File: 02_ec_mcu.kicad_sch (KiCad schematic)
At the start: 48 parts, among them J16 Case power/reset button harne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, J4 TC2030 Cortex SWD: VTref/SWDI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, SW1 Reset, SW4 BOOT0 (DFU), U4 STM32F407VGTx, U44 TCA9539PWR resettable source 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, U46 SN74LVC1G08DBVR EC-reset-qual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, U5 TPS54202DDC, Y1 J32SMX-K-F-G-I-8M0 8MHz CL8pF, Y2 X1A000141000612 32.768kHz CL6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

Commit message: Independent-verifier sweep: fix 12 stale contracts + 4 real board bugs
The full independent verification suite (not just the schematic gate)
caught real issues before routing:

Contracts/verifiers fixed (9 stale expectations that would have masked
regressions):
- U44 pin 9: SOURCE_MGR_SPARE2 -> SLS_S3 (contracts + closure)
- U61 pins 1/3/7: GND/NC -> EC_DFU_SEL / DFU DP/DM (DFU rework)
- C832 + U772 pins 1/2/4: SYS_3V3 -> PCIE_3V3_IN (endpoint buck)
- J2300: full 60-pin -> verified 30-pin FH12 map (contracts + pin review)
- J9 RTC header block -> D1824/C783 diode-OR block
- U63/R203 obsolete expectations (refs reused for the DFU parts)

Real board bugs found and fixed:
- J11 right-edge USB-C misplaced 6 mm inside the edge (shell pad would
  never align with the chassis cutout); moved to mirror J12 at x 353.48
- R207 fan PWM series resistor stranded at the right edge (shorted
  J11's shell); relocated under the NVMe card (height-legal), clear of
  the charger/mux clusters
- C35 placed inside the Ethernet notch void (would be routed off);
  moved to x 348
- BOM: 11 new parts missing Manufacturer/MPN stamps -> catalog entries
  added; BOM gate now PASS (0 gaps)

Release gate now: DRC all allowlisted (courtyards 165, silk 8+1),
schematic parity 0, pin review 2575 PASS / 0 FAIL, closure 1605/0,
calcs 123/0, off-board anchors 0. Remaining FAILs are expected:
stackup PENDING_NEXTPCB (awaiting fab reply) and 499 unrouted.
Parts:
- R212: MPN (none) -> RC0603FR-071KL; Manufacturer (none) -> Yageo
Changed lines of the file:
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@@
   (property "Footprint" "Resistor_SMD:R_0603_1608Metric" (at 20.32 229.87 0) (effects (font (size 1.27 1.27)) (hide yes)))
   (property "Datasheet" "" (at 20.32 229.87 0) (effects (font (size 1.27 1.27)) (hide yes)))
+  (property "Manufacturer" "Yageo" (at 20.32 229.87 0) (effects (font (size 1.27 1.27)) (hide yes)))
+  (property "MPN" "RC0603FR-071KL" (at 20.32 229.87 0) (effects (font (size 1.27 1.27)) (hide yes)))
   (pin "1")
   (pin "2")

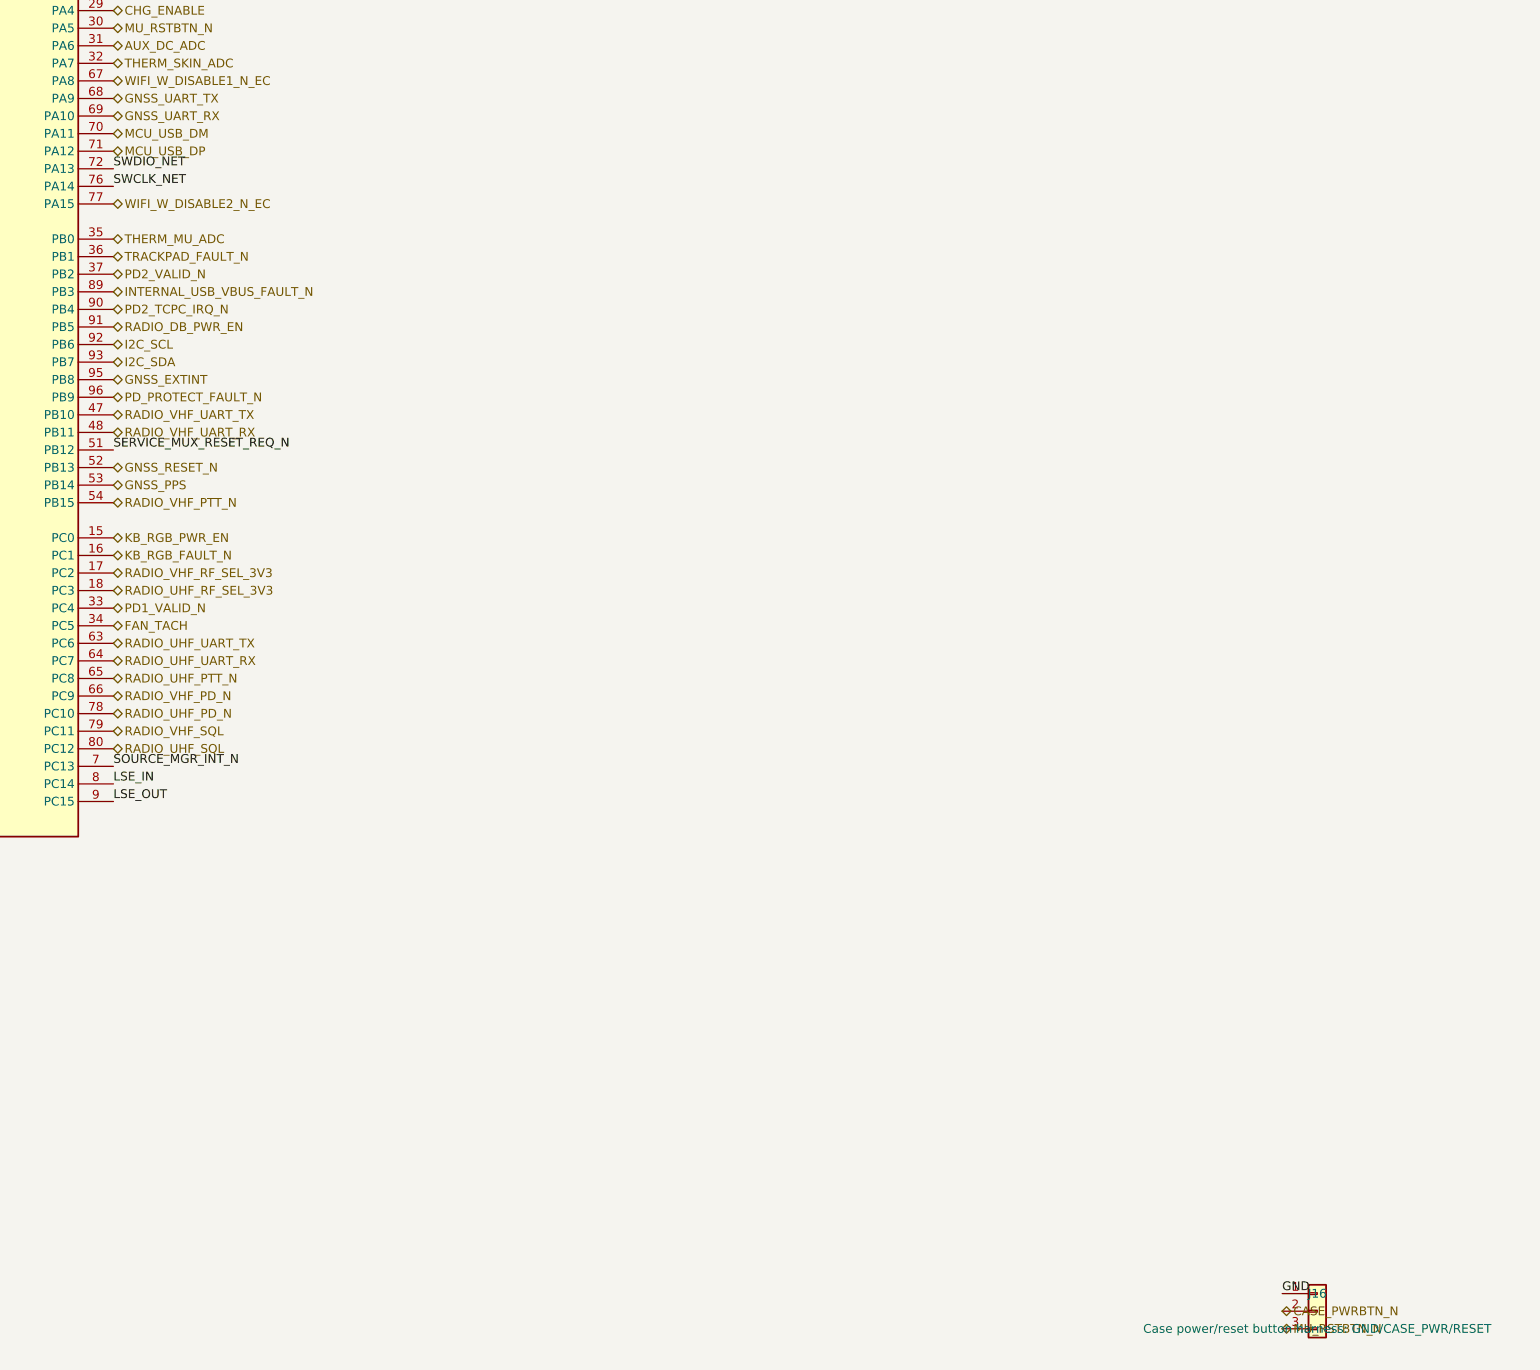
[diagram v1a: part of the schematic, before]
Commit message: get the main boards ready for routing
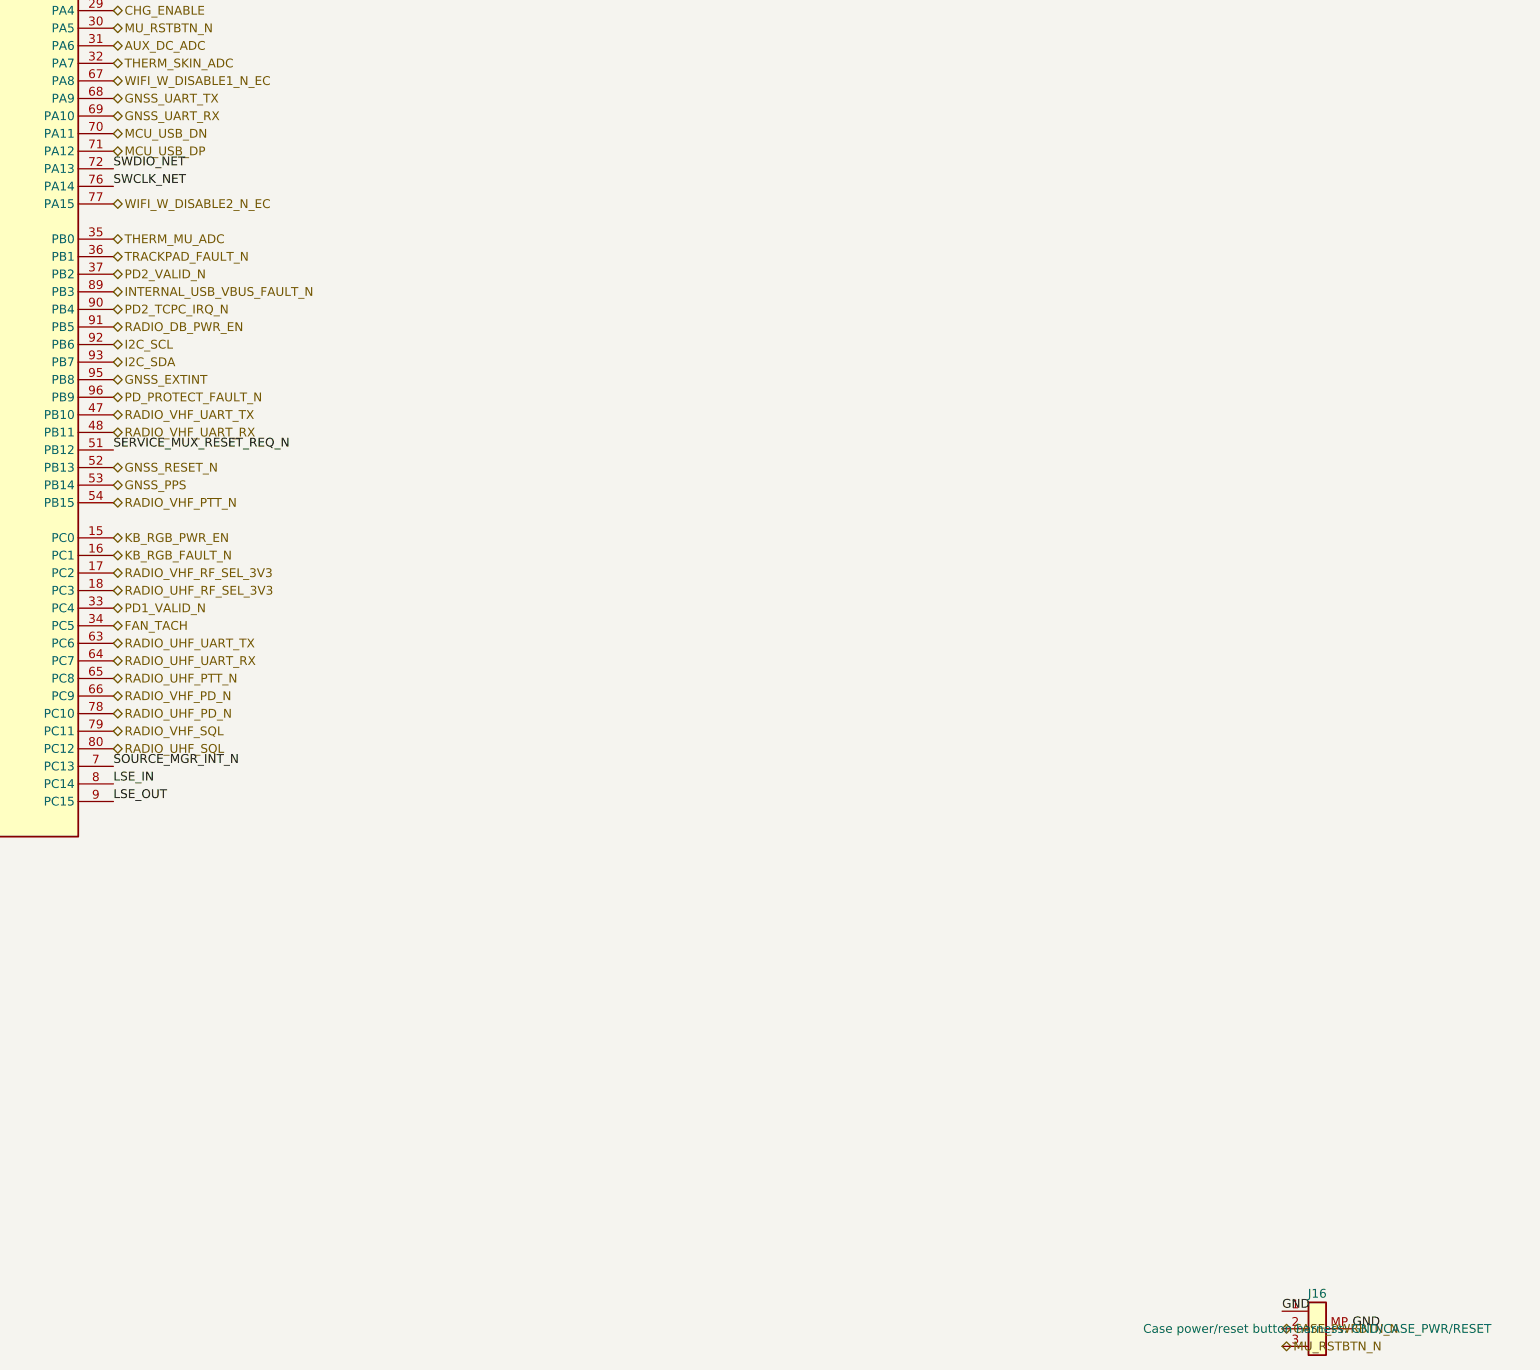
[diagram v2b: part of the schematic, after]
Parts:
- J16: symbol Connector_Generic:Conn_01x03 -> Conn_01x03_MP:Conn_01x03_MP
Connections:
- net GND: now also J16.MP
- net MCU_USB_DM renamed MCU_USB_DN
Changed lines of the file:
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@@
   (effects (font (size 1.27 1.27)) (justify left bottom))
 )
-(hierarchical_label "MCU_USB_DM"
+(hierarchical_label "MCU_USB_DN"
   (shape bidirectional)
   (at 275.59 364.49 0)
@@
 (text "== Final case controls (no exposed EC/service-map headers) ==" (at 449.58 260.35 0) (effects (font (size 1.27 1.27))))
 (symbol
-  (lib_id "Connector_Generic:Conn_01x03")
+  (lib_id "Conn_01x03_MP:Conn_01x03_MP")
   (at 449.58 534.67 0)
   (unit 1)
@@
   (pin "2")
   (pin "3")
+  (pin "MP")
   (instances
     (project "ducktop2"
@@
 )
 (label "GND"
-  (at 444.5 532.13 0)
+  (at 444.5 534.67 0)
   (effects (font (size 1.27 1.27)) (justify left bottom))
 )
 (hierarchical_label "CASE_PWRBTN_N"
   (shape bidirectional)
-  (at 444.5 534.67 0)
+  (at 444.5 537.21 0)
   (effects (font (size 1.27 1.27)) (justify left bottom))
 )
 (hierarchical_label "MU_RSTBTN_N"
   (shape bidirectional)
-  (at 444.5 537.21 0)
-  (effects (font (size 1.27 1.27)) (justify left bottom))
-)
+  (at 444.5 539.75 0)
+  (effects (font (size 1.27 1.27)) (justify left bottom))
+)
+(label "GND"
+  (at 454.66 537.21 0)
+  (effects (font (size 1.27 1.27)) (justify left bottom))
+)

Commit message: fix the center layout and more board issues
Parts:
- C291, C39: value 22u 16V X7R MCU_3V3 output -> 22u 25V X7R MCU_3V3 output; TI characterized part; footprint Capacitor_SMD:C_1206_3216Metric -> Capacitor_SMD:C_1210_3225Metric; MPN GRM31CZ71C226ME15L -> GRM32ER71E226KE15L
- L3: value 10uH 20% 3.3A Isat20 -> 10uH 20% 6.2A Isat30; 1.5A rail envelope; footprint ducktop2:Coilcraft_XGL5030 -> ducktop2:Coilcraft_XGL6030; MPN XGL5030-103MEC -> XGL6030-103MEC
- R35: value 100k 1% (3.3V FB hi) -> 100k 0.02% 5ppm MCU_3V3 FB hi; MPN RC0603FR-07100KL -> TNPU0603100KHZEN00; Manufacturer Yageo -> Vishay
- R36: value 22.1k 1% (3.3V FB lo) -> 22.1k 0.02% 5ppm MCU_3V3 FB lo; MPN RC0603FR-0722K1L -> TNPU060322K1HZEN00; Manufacturer Yageo -> Vishay
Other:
- note added: "== U5 TPS54202DDC EC_AON_IN -> MCU_3V3 buck; 1.5A continuous design envelope =="
- note removed: "== U5 TPS54202DDC EC_AON_IN -> MCU_3V3 Buck (3.3V, 2A) =="
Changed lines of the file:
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@@
   (effects (font (size 1.27 1.27)) (justify left bottom))
 )
-(text "== U5 TPS54202DDC EC_AON_IN -> MCU_3V3 Buck (3.3V, 2A) ==" (at 650.24 20.32 0) (effects (font (size 1.27 1.27))))
+(text "== U5 TPS54202DDC EC_AON_IN -> MCU_3V3 buck; 1.5A continuous design envelope ==" (at 650.24 20.32 0) (effects (font (size 1.27 1.27))))
 (symbol
   (lib_id "ducktop2:TPS54202DDC")
@@
   (dnp no)
   (property "Reference" "L3" (at 650.24 67.31 0) (effects (font (size 1.27 1.27))))
-  (property "Value" "10uH 20% 3.3A Isat20" (at 650.24 72.39 0) (effects (font (size 1.27 1.27))))
-  (property "Footprint" "ducktop2:Coilcraft_XGL5030" (at 650.24 69.85 0) (effects (font (size 1.27 1.27)) (hide yes)))
+  (property "Value" "10uH 20% 6.2A Isat30; 1.5A rail envelope" (at 650.24 72.39 0) (effects (font (size 1.27 1.27))))
+  (property "Footprint" "ducktop2:Coilcraft_XGL6030" (at 650.24 69.85 0) (effects (font (size 1.27 1.27)) (hide yes)))
   (property "Datasheet" "" (at 650.24 69.85 0) (effects (font (size 1.27 1.27)) (hide yes)))
   (property "Manufacturer" "Coilcraft" (at 650.24 69.85 0) (effects (font (size 1.27 1.27)) (hide yes)))
-  (property "MPN" "XGL5030-103MEC" (at 650.24 69.85 0) (effects (font (size 1.27 1.27)) (hide yes)))
-  (property "Datasheet" "https://www.coilcraft.com/getmedia/e64ac115-95f2-45c7-b798-1b3769b91583/xgl5030.pdf" (at 650.24 69.85 0) (effects (font (size 1.27 1.27)) (hide yes)))
+  (property "MPN" "XGL6030-103MEC" (at 650.24 69.85 0) (effects (font (size 1.27 1.27)) (hide yes)))
+  (property "Datasheet" "https://www.coilcraft.com/getmedia/9bfb2606-51aa-49a6-98ad-d20f3504c8ae/xgl6030.pdf" (at 650.24 69.85 0) (effects (font (size 1.27 1.27)) (hide yes)))
   (pin "1")
   (pin "2")
@@
   (dnp no)
   (property "Reference" "R35" (at 650.24 77.47 0) (effects (font (size 1.27 1.27))))
-  (property "Value" "100k 1% (3.3V FB hi)" (at 650.24 82.55 0) (effects (font (size 1.27 1.27))))
+  (property "Value" "100k 0.02% 5ppm MCU_3V3 FB hi" (at 650.24 82.55 0) (effects (font (size 1.27 1.27))))
   (property "Footprint" "Resistor_SMD:R_0603_1608Metric" (at 650.24 80.01 0) (effects (font (size 1.27 1.27)) (hide yes)))
   (property "Datasheet" "" (at 650.24 80.01 0) (effects (font (size 1.27 1.27)) (hide yes)))
-  (property "Manufacturer" "Yageo" (at 650.24 80.01 0) (effects (font (size 1.27 1.27)) (hide yes)))
-  (property "MPN" "RC0603FR-07100KL" (at 650.24 80.01 0) (effects (font (size 1.27 1.27)) (hide yes)))
+  (property "Manufacturer" "Vishay" (at 650.24 80.01 0) (effects (font (size 1.27 1.27)) (hide yes)))
+  (property "MPN" "TNPU0603100KHZEN00" (at 650.24 80.01 0) (effects (font (size 1.27 1.27)) (hide yes)))
   (pin "1")
   (pin "2")
@@
   (dnp no)
   (property "Reference" "R36" (at 650.24 87.63 0) (effects (font (size 1.27 1.27))))
-  (property "Value" "22.1k 1% (3.3V FB lo)" (at 650.24 92.71 0) (effects (font (size 1.27 1.27))))
+  (property "Value" "22.1k 0.02% 5ppm MCU_3V3 FB lo" (at 650.24 92.71 0) (effects (font (size 1.27 1.27))))
   (property "Footprint" "Resistor_SMD:R_0603_1608Metric" (at 650.24 90.17 0) (effects (font (size 1.27 1.27)) (hide yes)))
   (property "Datasheet" "" (at 650.24 90.17 0) (effects (font (size 1.27 1.27)) (hide yes)))
-  (property "Manufacturer" "Yageo" (at 650.24 90.17 0) (effects (font (size 1.27 1.27)) (hide yes)))
-  (property "MPN" "RC0603FR-0722K1L" (at 650.24 90.17 0) (effects (font (size 1.27 1.27)) (hide yes)))
+  (property "Manufacturer" "Vishay" (at 650.24 90.17 0) (effects (font (size 1.27 1.27)) (hide yes)))
+  (property "MPN" "TNPU060322K1HZEN00" (at 650.24 90.17 0) (effects (font (size 1.27 1.27)) (hide yes)))
   (pin "1")
   (pin "2")
@@
   (dnp no)
   (property "Reference" "C39" (at 650.24 97.79 0) (effects (font (size 1.27 1.27))))
-  (property "Value" "22u 16V X7R MCU_3V3 output" (at 650.24 102.87 0) (effects (font (size 1.27 1.27))))
-  (property "Footprint" "Capacitor_SMD:C_1206_3216Metric" (at 650.24 100.33 0) (effects (font (size 1.27 1.27)) (hide yes)))
+  (property "Value" "22u 25V X7R MCU_3V3 output; TI characterized part" (at 650.24 102.87 0) (effects (font (size 1.27 1.27))))
+  (property "Footprint" "Capacitor_SMD:C_1210_3225Metric" (at 650.24 100.33 0) (effects (font (size 1.27 1.27)) (hide yes)))
   (property "Datasheet" "" (at 650.24 100.33 0) (effects (font (size 1.27 1.27)) (hide yes)))
   (property "Manufacturer" "Murata" (at 650.24 100.33 0) (effects (font (size 1.27 1.27)) (hide yes)))
-  (property "MPN" "GRM31CZ71C226ME15L" (at 650.24 100.33 0) (effects (font (size 1.27 1.27)) (hide yes)))
+  (property "MPN" "GRM32ER71E226KE15L" (at 650.24 100.33 0) (effects (font (size 1.27 1.27)) (hide yes)))
   (pin "1")
   (pin "2")
@@
   (dnp no)
   (property "Reference" "C291" (at 650.24 107.95 0) (effects (font (size 1.27 1.27))))
-  (property "Value" "22u 16V X7R MCU_3V3 output" (at 650.24 113.03 0) (effects (font (size 1.27 1.27))))
-  (property "Footprint" "Capacitor_SMD:C_1206_3216Metric" (at 650.24 110.49 0) (effects (font (size 1.27 1.27)) (hide yes)))
+  (property "Value" "22u 25V X7R MCU_3V3 output; TI characterized part" (at 650.24 113.03 0) (effects (font (size 1.27 1.27))))
+  (property "Footprint" "Capacitor_SMD:C_1210_3225Metric" (at 650.24 110.49 0) (effects (font (size 1.27 1.27)) (hide yes)))
   (property "Datasheet" "" (at 650.24 110.49 0) (effects (font (size 1.27 1.27)) (hide yes)))
   (property "Manufacturer" "Murata" (at 650.24 110.49 0) (effects (font (size 1.27 1.27)) (hide yes)))
-  (property "MPN" "GRM31CZ71C226ME15L" (at 650.24 110.49 0) (effects (font (size 1.27 1.27)) (hide yes)))
-  (pin "1")
-  (pin "2")
+  (property "MPN" "GRM32ER71E226KE15L" (at 650.24 110.49 0) (effects (font (size 1.27 1.27)) (hide yes)))
+  (pin "1")
+  (pin "2")
